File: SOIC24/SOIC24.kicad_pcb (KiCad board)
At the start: 2 copper layers, 23.1 x 30.7 mm, 8 parts, among them J1 Conn_01x12, J2 Conn_02x12_Counter_Clockwise, J3 Conn_02x12_Counter_Clockwise, J4 Conn_02x12_Counter_Clockwise, J5 Conn_01x12

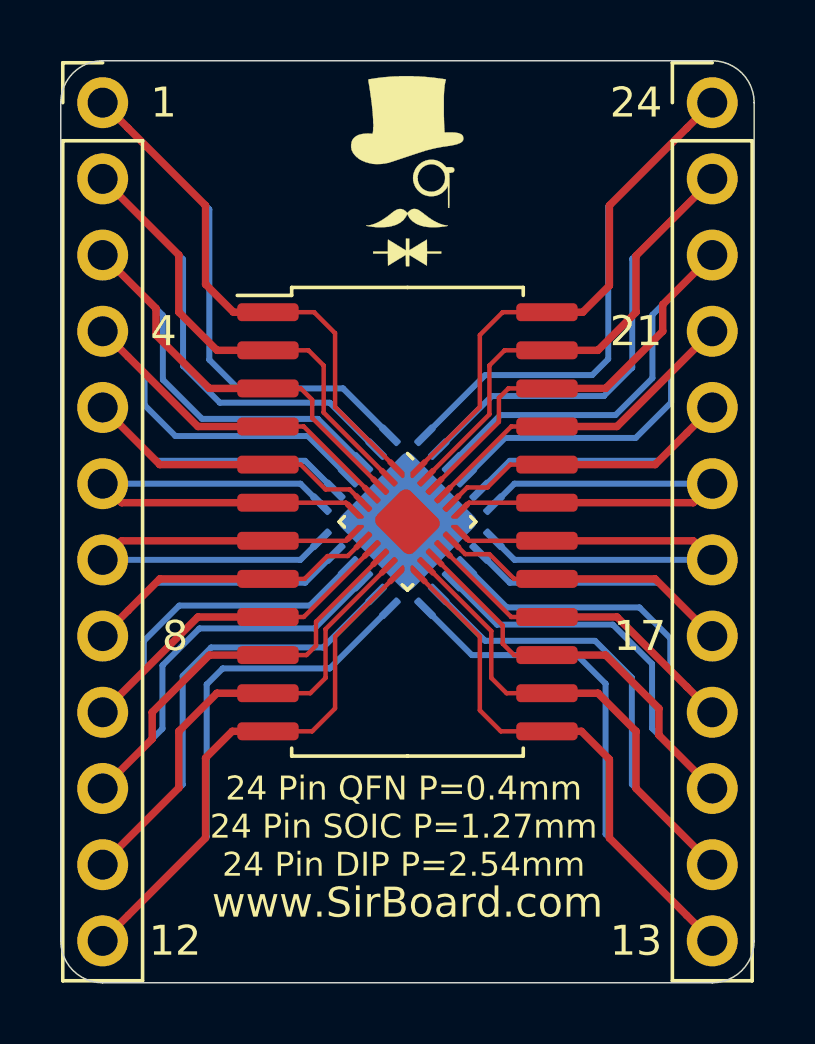
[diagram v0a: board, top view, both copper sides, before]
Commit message: Silkscreens and sizes updated
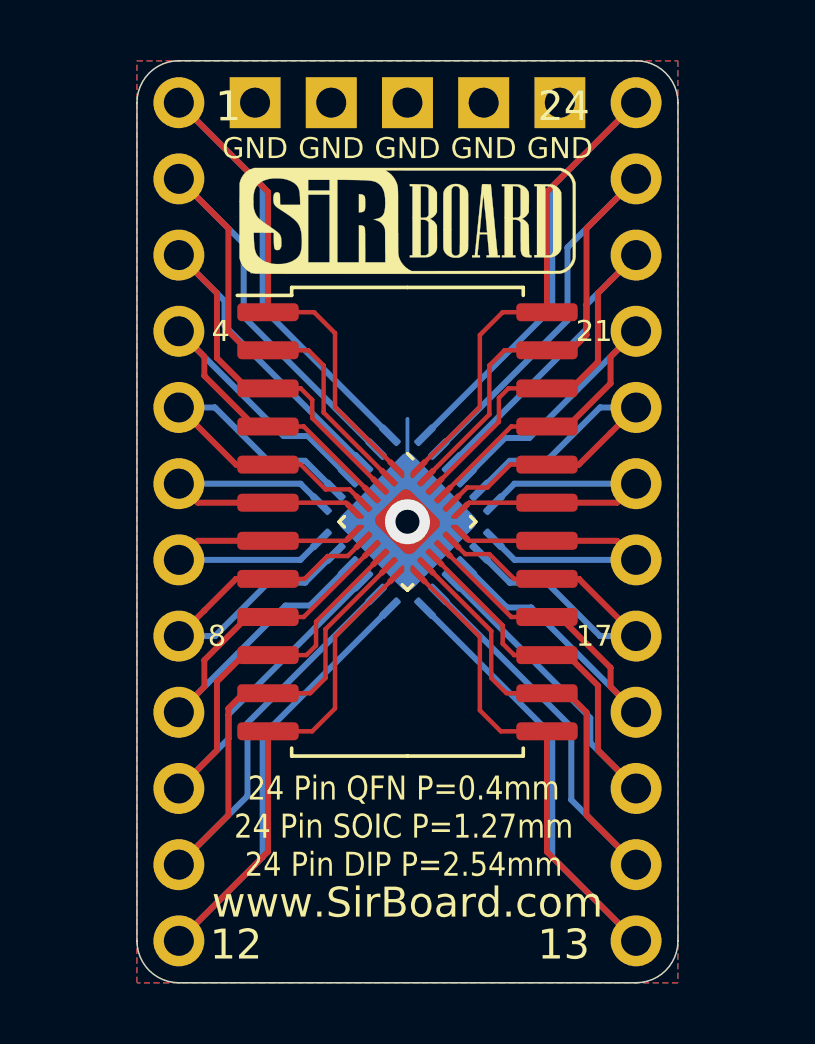
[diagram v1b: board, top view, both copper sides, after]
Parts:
- removed the G*** at (198.1, 110.2)
- removed the G*** at (198.1, 131.4)
- added G***: LOGO, logo:logo76x107, B.Cu at (198.1, 129.7)
- added G***: LOGO, logo:SirBoard112x35, F.Cu at (198.1, 111.9)
- added J6: Conn_01x05, Connector_PinHeader_2.54mm:PinHeader_1x05_P2.54mm_Vertical, B.Cu at (193.0, 108.0)
- J1, J5: moved to B.Cu
- moved J1 2.54 mm to (190.5, 108.0), turned to 180 degrees
- moved J5 2.54 mm to (205.7, 108.0), turned to 180 degrees
- moved G*** 1.65 mm to (198.1, 115.6), turned to 180 degrees
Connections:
- J2 pad 25: (no net) -> Net-(J6-Pad1)
- J4 pad 25: (no net) -> Net-(J6-Pad1)
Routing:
- net Net-(J2-Pad16): track 21.9 -> 16.7 mm
- net Net-(J1-Pad4): track 21.9 -> 16.7 mm
- net Net-(J2-Pad21): track 21.9 -> 16.9 mm
- net Net-(J1-Pad9): track 21.9 -> 16.9 mm
- net Net-(J1-Pad3): track 25.9 -> 21.0 mm
- net Net-(J2-Pad15): track 25.9 -> 21.0 mm
- net Net-(J2-Pad19): track 16.2 -> 11.3 mm
- net Net-(J2-Pad18): track 16.2 -> 11.3 mm
- net Net-(J2-Pad20): track 18.7 -> 13.8 mm
- net Net-(J2-Pad17): track 18.7 -> 13.8 mm
- net Net-(J1-Pad8): track 18.7 -> 13.8 mm
- net Net-(J1-Pad5): track 18.7 -> 13.8 mm
- net Net-(J1-Pad7): track 16.2 -> 11.3 mm
- net Net-(J1-Pad6): track 16.2 -> 11.3 mm
- net Net-(J2-Pad22): track 26.0 -> 21.2 mm
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- added copper zone on B.Cu, net Net-(J6-Pad1)
- added copper zone on F.Cu, net Net-(J6-Pad1)
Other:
- board size 23.1 x 30.7 mm -> 18 x 30.7 mm
- board text added: "GND"

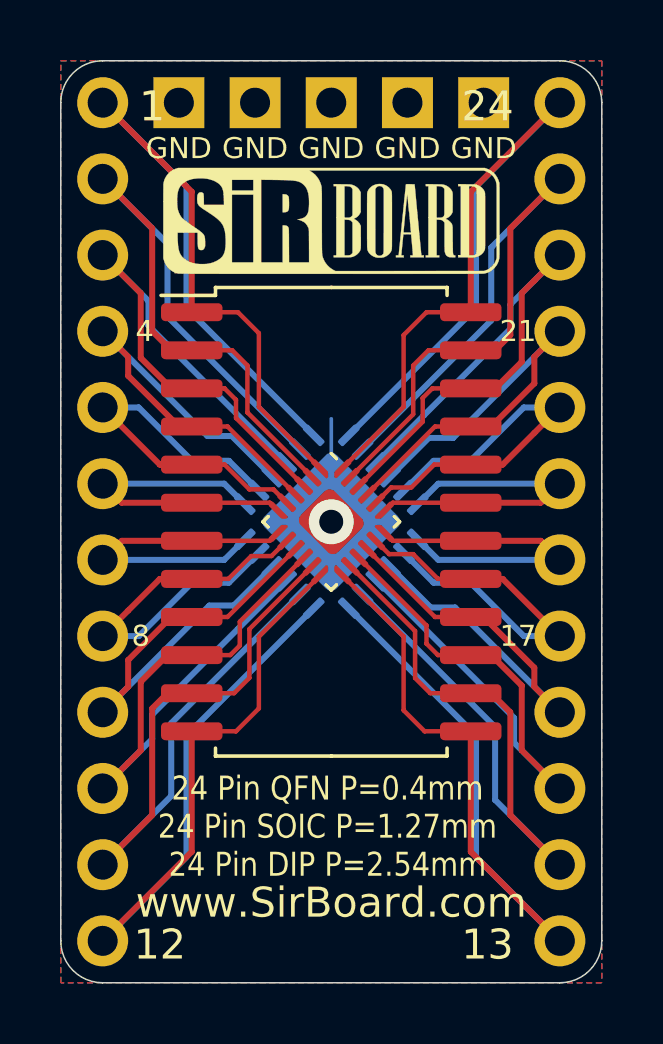
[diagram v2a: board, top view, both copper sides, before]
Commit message: Pin Numbering edited
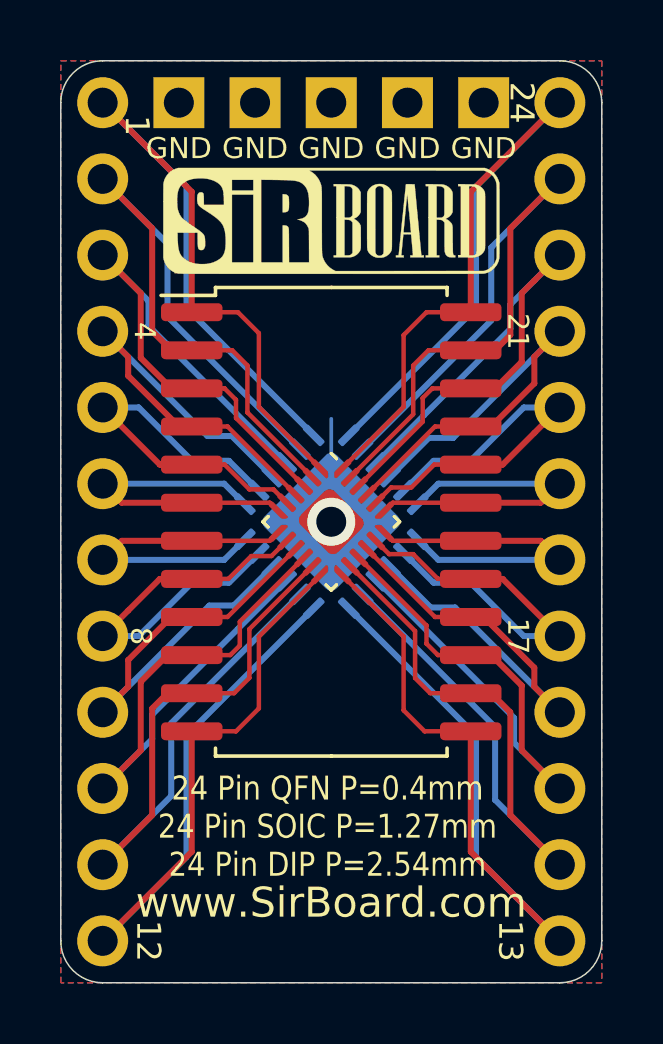
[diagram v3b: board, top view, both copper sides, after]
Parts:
- J1, J5, J6: moved to F.Cu
- turned J1 to 0 degrees
- turned J5 to 0 degrees
- turned J6 to 90 degrees

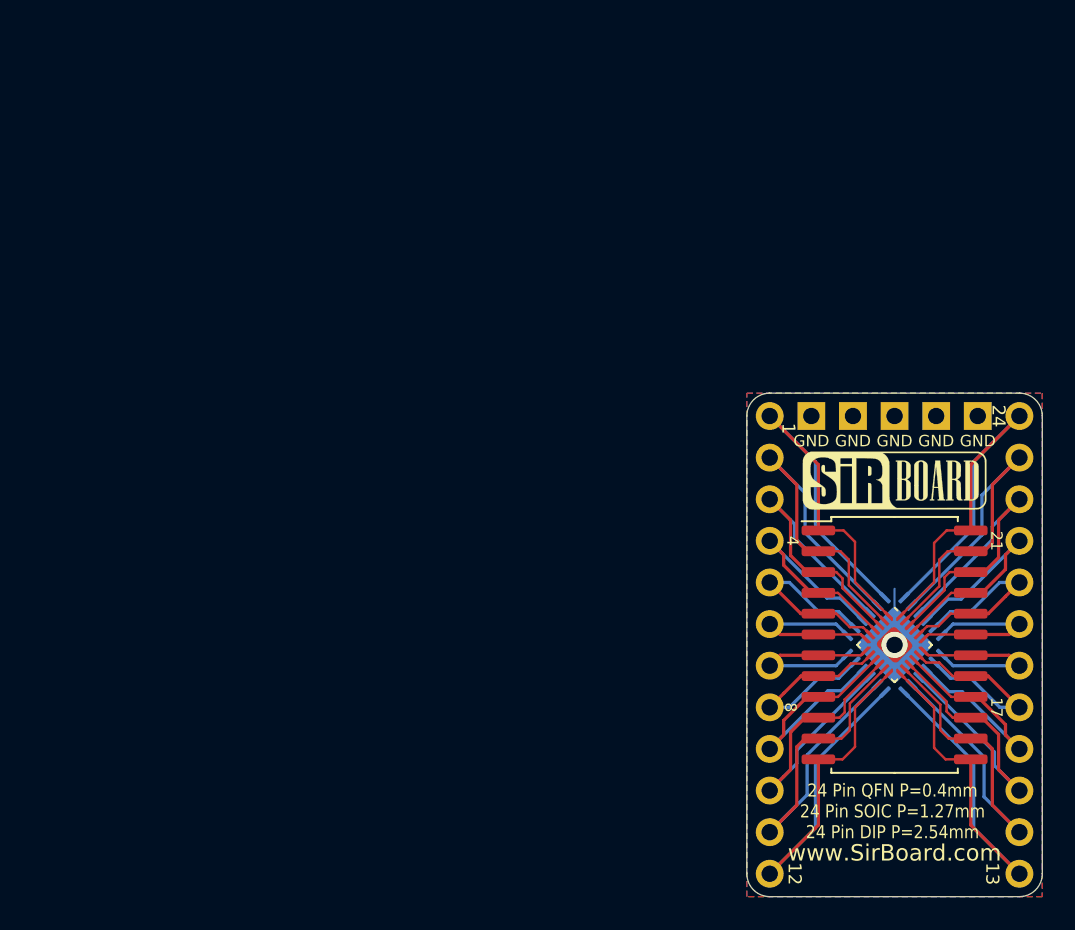
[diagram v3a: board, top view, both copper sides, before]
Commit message: Numbering Orientation Edited
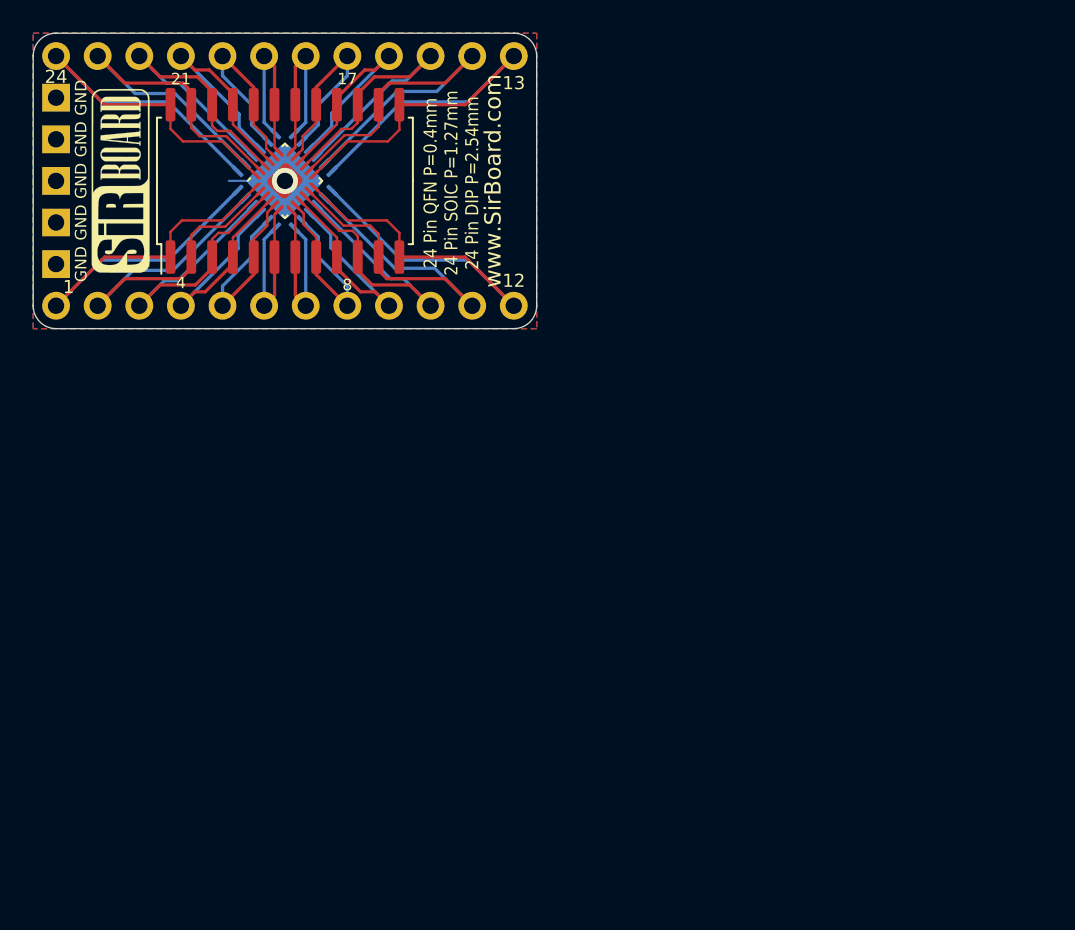
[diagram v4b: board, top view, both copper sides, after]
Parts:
- removed the G*** at (198.1, 129.7)
- added G***: LOGO, logo:logo94x134, B.Cu at (168.4, 93.6)
- moved J5 62.8 mm to (146.9, 86.0), turned to 90 degrees
- moved G*** 50.7 mm to (150.9, 93.6), turned to 90 degrees
- moved G*** 48.8 mm to (154.6, 93.6), turned to 270 degrees
- moved J6 47.0 mm to (146.9, 98.7), turned to 180 degrees
- moved J2 46.8 mm to (160.9, 93.6), turned to 45 degrees
- moved J3 46.8 mm to (160.9, 93.6), turned to 90 degrees
- moved J4 46.8 mm to (160.9, 93.6), turned to 315 degrees
- moved J1 44.1 mm to (146.9, 101.2), turned to 90 degrees
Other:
- board size 18 x 30.7 mm -> 30.7 x 18 mm

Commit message: Silkscreen Edits
Dimensions moved to Drawings Layer
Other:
- rule pad_to_mask_clearance: 0.051 -> 0
- rule solder_mask_min_width: 0.25 -> 0.1
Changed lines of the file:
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@@
     (38 B.Mask user)
     (39 F.Mask user)
-    (40 Dwgs.User user hide)
+    (40 Dwgs.User user)
     (41 Cmts.User user hide)
     (42 Eco1.User user hide)
@@
     (pad_size 3.4 3.4)
     (pad_drill 0)
-    (pad_to_mask_clearance 0.051)
-    (solder_mask_min_width 0.25)
+    (pad_to_mask_clearance 0)
+    (solder_mask_min_width 0.1)
     (aux_axis_origin 0 0)
     (visible_elements 7FFFFFFF)
     (pcbplotparams
-      (layerselection 0x010fc_ffffffff)
+      (layerselection 0x010f0_ffffffff)
       (usegerberextensions false)
       (usegerberattributes false)
@@
       (linewidth 0.100000)
       (plotframeref false)
-      (viasonmask false)
+      (viasonmask true)
       (mode 1)
-      (useauxorigin false)
+      (useauxorigin true)
       (hpglpennumber 1)
       (hpglpenspeed 20)
@@
       (psa4output false)
       (plotreference true)
-      (plotvalue true)
+      (plotvalue false)
       (plotinvisibletext false)
       (padsonsilk false)
@@
       (outputformat 1)
       (mirror false)
-      (drillshape 1)
+      (drillshape 0)
       (scaleselection 1)
-      (outputdirectory ""))
+      (outputdirectory "../../Gerbers/SOIC24/"))
   )
   (net 0 "")
@@
     (effects (font (size 0.7 0.7) (thickness 0.12)))
   )
-  (dimension 27.94 (width 0.15) (layer F.SilkS)
-    (gr_text "27.940 mm" (at 160.909 81.25) (layer F.SilkS)
+  (dimension 27.94 (width 0.15) (layer Dwgs.User)
+    (gr_text "27.940 mm" (at 160.909 81.25) (layer Dwgs.User)
       (effects (font (size 1 1) (thickness 0.15)) hide)
     )
@@
     (arrow2b (pts (xy 146.939 82.55) (xy 148.065504 81.963579)))
   )
-  (dimension 30.734 (width 0.15) (layer F.SilkS)
-    (gr_text "30.734 mm" (at 160.909 78.202) (layer F.SilkS)
+  (dimension 30.734 (width 0.15) (layer Dwgs.User)
+    (gr_text "30.734 mm" (at 160.909 78.202) (layer Dwgs.User)
       (effects (font (size 1 1) (thickness 0.15)) hide)
     )
@@
     (arrow2b (pts (xy 145.542 79.502) (xy 146.668504 78.915579)))
   )
-  (dimension 15.24 (width 0.15) (layer F.SilkS)
-    (gr_text "15.240 mm" (at 142.21 93.599 90) (layer F.SilkS)
+  (dimension 15.24 (width 0.15) (layer Dwgs.User)
+    (gr_text "15.240 mm" (at 142.21 93.599 90) (layer Dwgs.User)
       (effects (font (size 1 1) (thickness 0.15)) hide)
     )
@@
     (arrow2b (pts (xy 143.51 101.219) (xy 142.923579 100.092496)))
   )
-  (dimension 18.034 (width 0.15) (layer F.SilkS)
-    (gr_text "18.034 mm" (at 139.035 93.599 90) (layer F.SilkS)
+  (dimension 18.034 (width 0.15) (layer Dwgs.User)
+    (gr_text "18.034 mm" (at 139.035 93.599 90) (layer Dwgs.User)
       (effects (font (size 1 1) (thickness 0.15)) hide)
     )

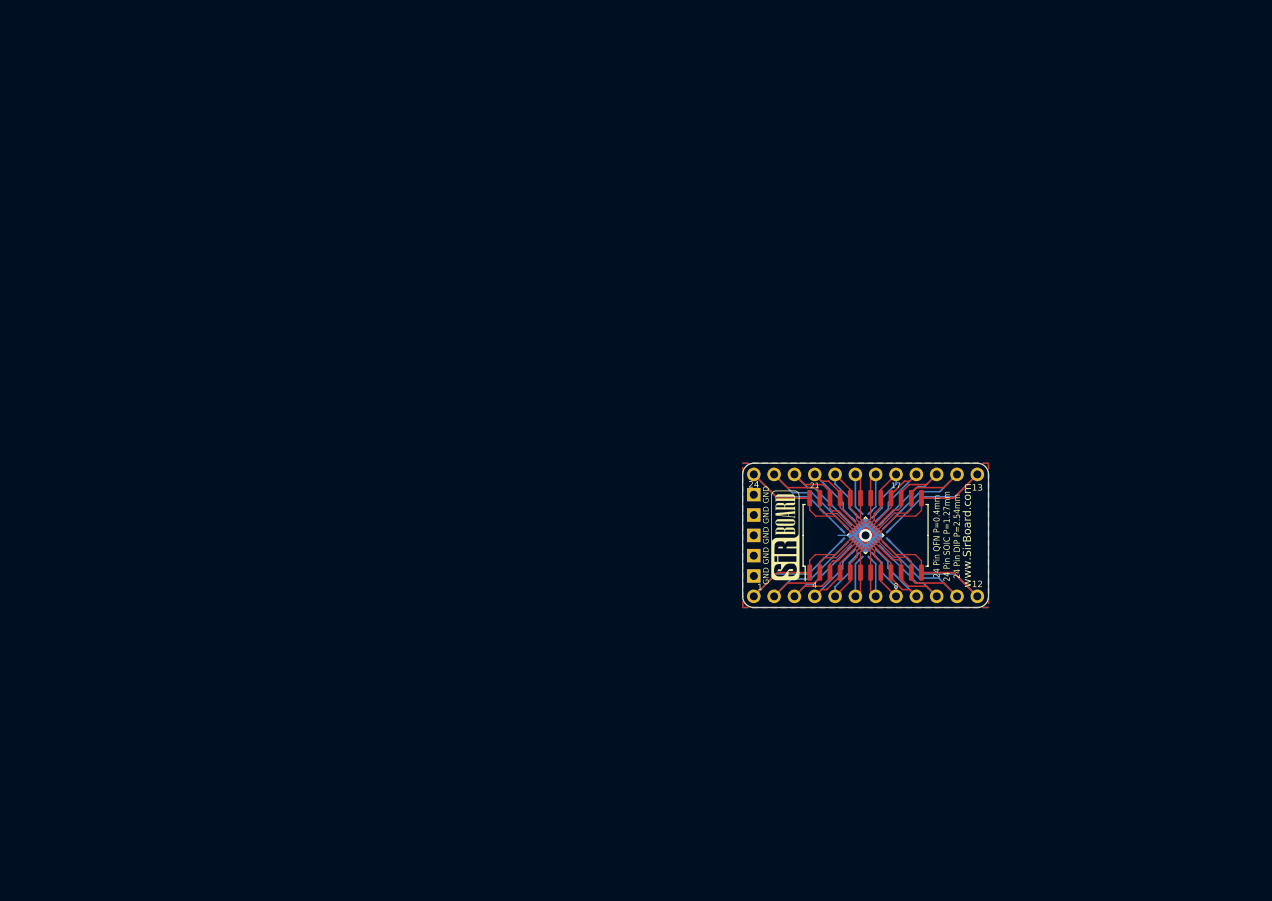
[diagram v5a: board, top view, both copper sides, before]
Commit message: USB, SD and CR Cells Added
MicroSD, MicroUSB, MiniUSB, USB-C, CR1220, CR2032 added as well as all schematics page sizes optimised
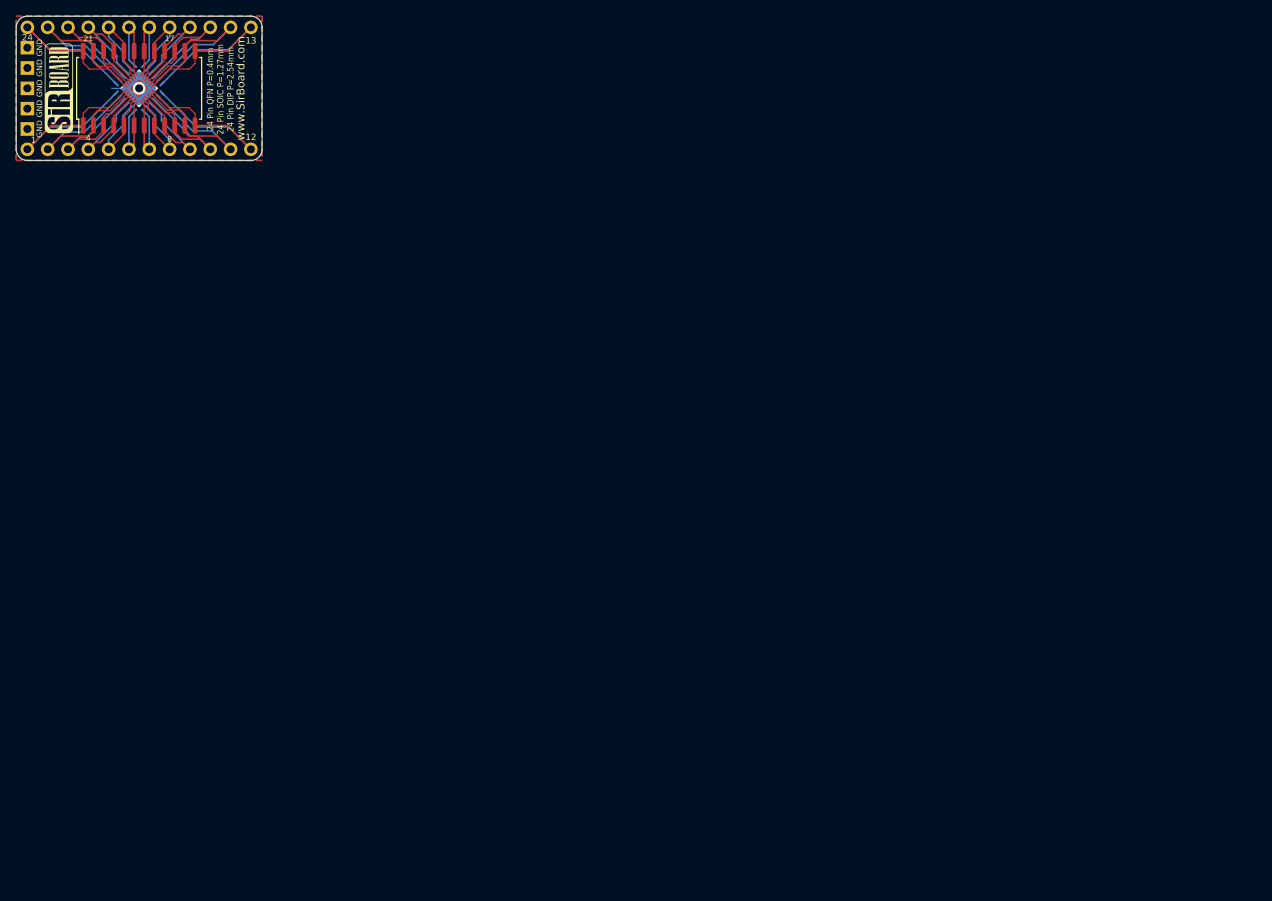
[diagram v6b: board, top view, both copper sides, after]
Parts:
- moved G*** 106.6 mm to (60.1, 37.7)
- moved G*** 106.6 mm to (63.8, 37.7)
- moved G*** 106.6 mm to (77.6, 37.7)
- moved J1 106.6 mm to (56.1, 45.3)
- moved J2 106.6 mm to (70.1, 37.7)
- moved J3 106.6 mm to (70.1, 37.7)
- moved J4 106.6 mm to (70.1, 37.7)
- moved J5 106.6 mm to (56.1, 30.1)
- moved J6 106.6 mm to (56.1, 42.8)

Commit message: Board Updates
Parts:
- G***: footprint logo:logo94x134 -> logo:logo76x107
- moved G*** 0.38 mm to (78.0, 37.7), turned to 270 degrees
- moved G*** 0.13 mm to (63.9, 37.7)
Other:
- board size 30.7 x 18 mm -> 30.5 x 17.8 mm
